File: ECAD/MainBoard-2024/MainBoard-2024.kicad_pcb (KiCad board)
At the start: 2 copper layers, 60 x 150 mm, 82 parts, among them J1 XT60, J10 Conn_01x14, J11 Conn_01x03, J12 Conn_01x04, J13 Conn_01x03, J14 Conn_01x03, J16 XT30, J17 XT30, J2 Conn_01x04, J20 BAU, J21 BAU, J22 Conn_01x04, J23 Conn_01x02, J26 BAU, J27 BAU, J28 Conn_01x02, J29 Conn_01x02, J3 ConStep1, J30 Conn_01x03, J5 ConStep1, J6 ConStep1, J7 XT30, J8 Conn_01x02, J9 XT60, K1 CB1-P-24V, U1 Teensy3.5_All_Pins, U2 R-78B3.3-2.0, U3 PCA9685PW, U4 R-78B5.0-2.0

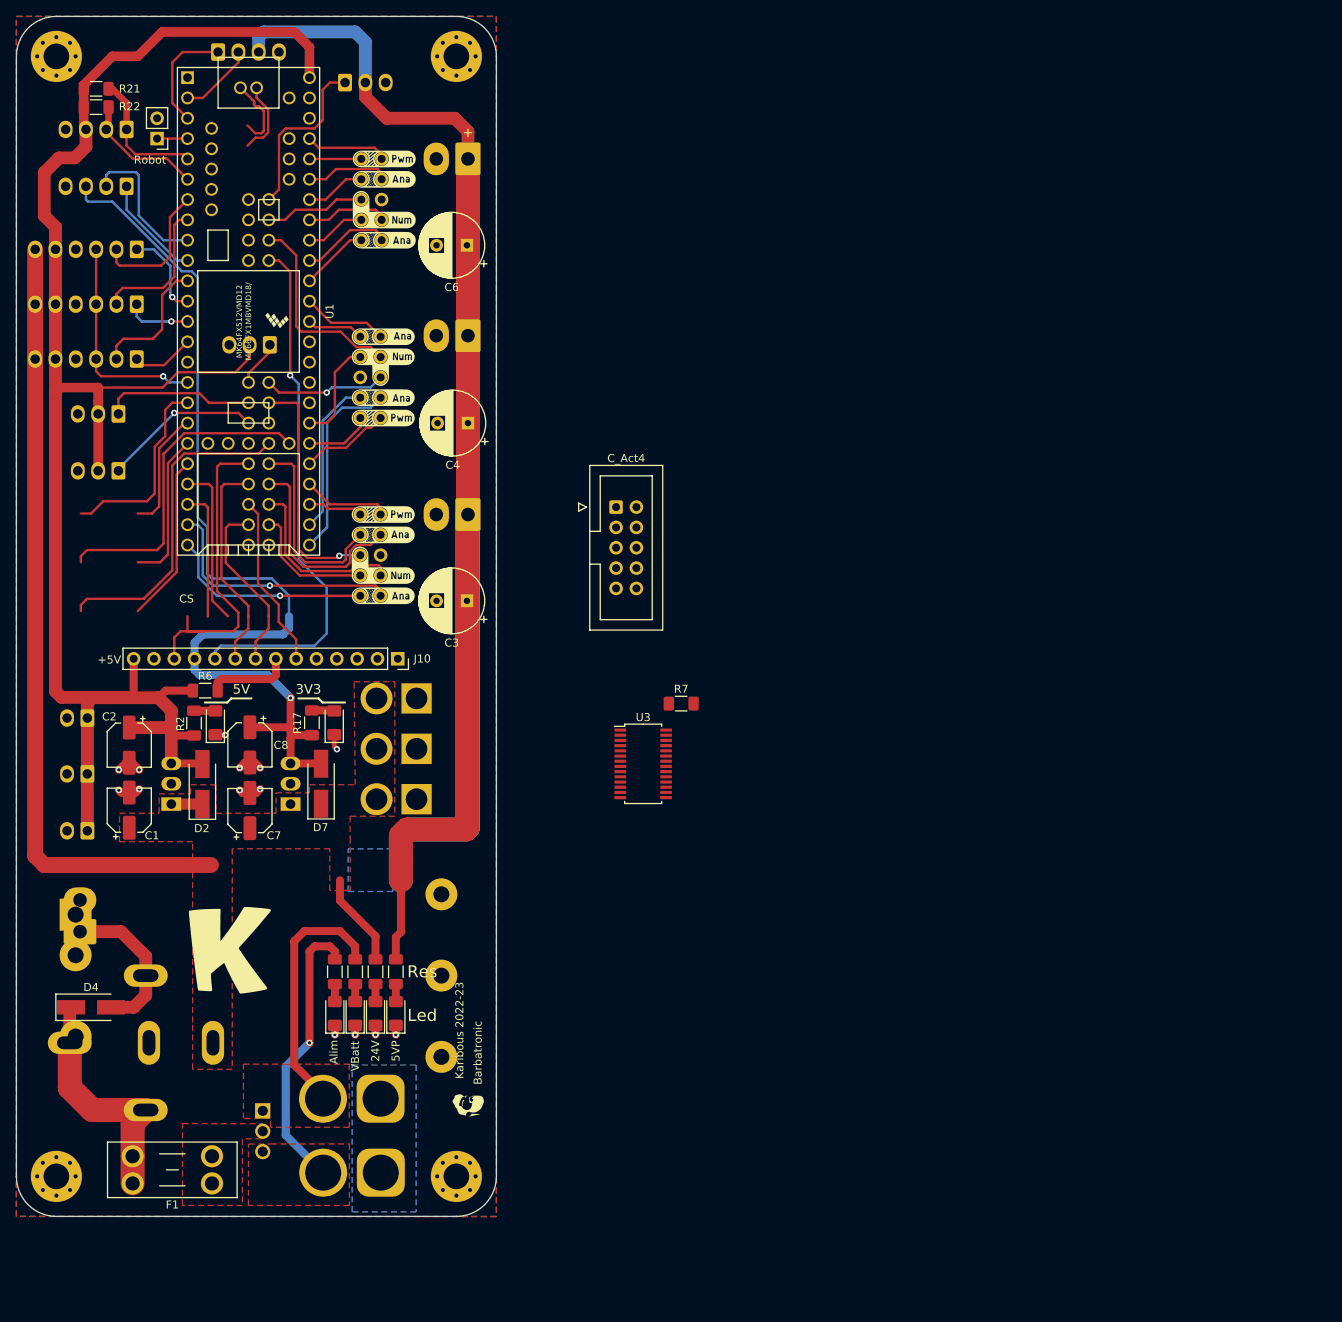
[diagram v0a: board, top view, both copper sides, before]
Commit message: update component and edge cut
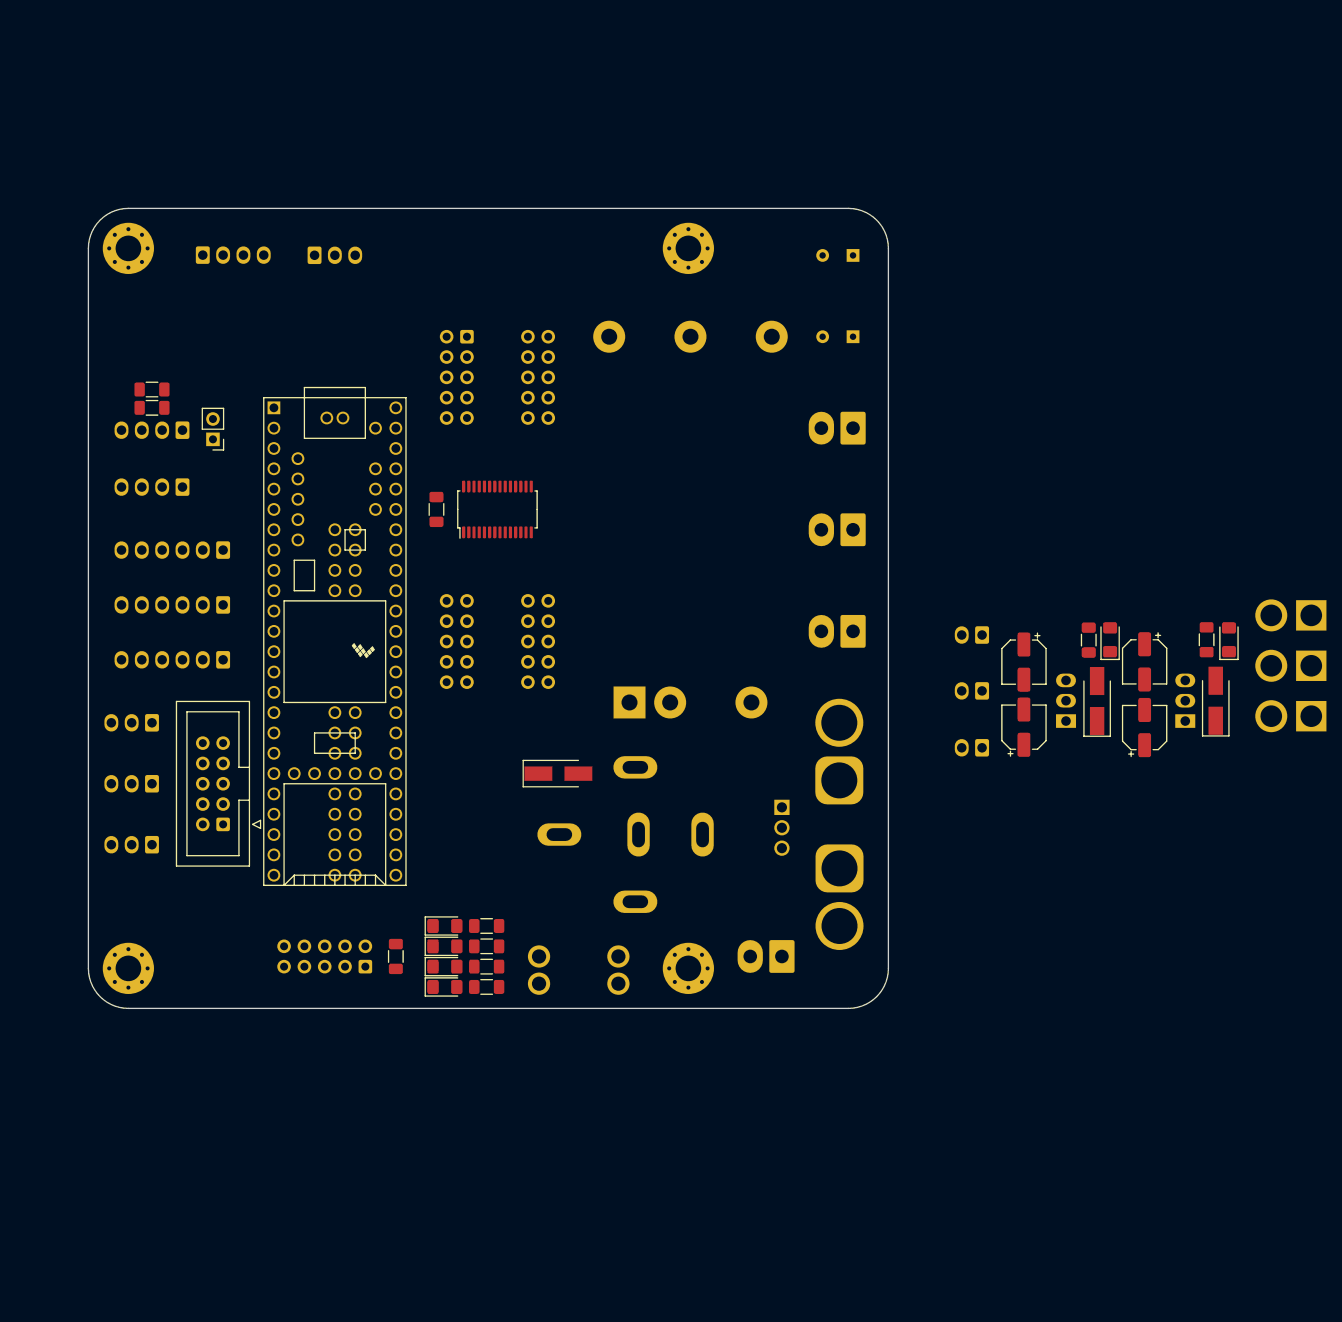
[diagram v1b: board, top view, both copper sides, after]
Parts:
- removed C3: 220uF, Capacitor_THT:CP_Radial_D8.0mm_P3.80mm
- removed G*** (x13): LOGO, LOGO
- removed J10: Conn_01x14, Connector_PinSocket_2.54mm:PinSocket_1x14_P2.54mm_Vertical
- removed kibuzzard-62E65D6B: G***, kibuzzard-62E65D6B
- removed kibuzzard-62E65D77: G***, kibuzzard-62E65D77
- removed kibuzzard-62E65D7D: G***, kibuzzard-62E65D7D
- added Con-TFT1: Conn_02x05_Odd_Even, Connector_IDC:IDC-Header_2x05_P2.54mm_Vertical, B.Cu at (134.6, 144.8)
- added IHM-IO1: Conn_02x05_Odd_Even, Connector_IDC:IDC-Header_2x05_P2.54mm_Vertical, F.Cu at (116.8, 127.0)
- C4, C6, C_Act4, F1: moved to B.Cu
- moved D2 112.3 mm to (226.1, 111.6)
- moved D3 112.3 mm to (227.7, 103.9)
- moved D7 112.3 mm to (240.9, 111.5)
- moved R17 112.3 mm to (239.8, 103.9)
- moved R2 112.3 mm to (225.0, 104.0)
- moved U2 112.3 mm to (237.1, 114.1)
- moved U4 112.3 mm to (222.2, 114.1)
- moved C1 112.3 mm to (216.9, 114.8)
- moved C2 112.3 mm to (216.9, 106.7)
- moved C7 112.3 mm to (232.0, 114.9)
- moved C8 112.3 mm to (232.0, 106.7)
- moved J23 112.3 mm to (211.7, 110.3)
- moved J28 112.3 mm to (211.7, 117.4)
- moved J29 112.3 mm to (211.7, 103.3)
- moved D8 112.3 mm to (242.6, 103.9)
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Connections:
- C_Act1 pad 1: C_Act1-1 -> Act1_01
- C_Act1 pad 10: C_Act1-8 -> Servo03
- C_Act1 pad 2: C_Act1-2 -> Servo00
- C_Act1 pad 3: C_Act1-3 -> Act1_02
- C_Act1 pad 4: C_Act1-4 -> Servo01
- C_Act1 pad 5: C_Act1-9 -> Act1_03
- C_Act1 pad 7: C_Act1-5 -> Act1_04
- C_Act1 pad 8: C_Act1-6 -> Servo02
- C_Act1 pad 9: C_Act1-7 -> Act1_05
- C_Act2 pad 1: C_Act2-8 -> Act2_01
- C_Act2 pad 10: C_Act2-1 -> Servo07
- C_Act2 pad 2: C_Act2-7 -> Servo04
- C_Act2 pad 3: C_Act2-6 -> Act2_02
- C_Act2 pad 4: C_Act2-5 -> Servo05
- C_Act2 pad 5: C_Act2-9 -> Act2_03
- C_Act2 pad 7: C_Act2-4 -> Act2_04
- C_Act2 pad 8: C_Act2-3 -> Servo06
- C_Act2 pad 9: C_Act2-2 -> Act2_05
- C_Act3 pad 1: C_Act3-1 -> Act3_01
- C_Act3 pad 10: C_Act3-8 -> Servo11
- C_Act3 pad 2: C_Act3-2 -> Servo08
- C_Act3 pad 3: C_Act3-3 -> Act3_02
- C_Act3 pad 4: C_Act3-4 -> Servo09
- C_Act3 pad 5: C_Act3-9 -> Act3_03
- C_Act3 pad 7: C_Act3-5 -> Act3_04
- C_Act3 pad 8: C_Act3-6 -> Servo10
- C_Act3 pad 9: C_Act3-7 -> Act3_05
- C_Act4 pad 1: Reset -> Act4_01
- C_Act4 pad 10: unconnected-(C_Act4-Pin_10-Pad10) -> Servo15
- C_Act4 pad 2: Init -> Servo12
- C_Act4 pad 3: Program -> Act4_02
- C_Act4 pad 4: unconnected-(C_Act4-Pin_4-Pad4) -> Servo13
- C_Act4 pad 5: Detection -> Act4_03
- C_Act4 pad 7: Couleur -> Act4_04
- C_Act4 pad 8: unconnected-(C_Act4-Pin_8-Pad8) -> Servo14
- C_Act4 pad 9: Tirette -> Act4_05
- U1 pad 23: C_Act3-2 -> unconnected-(U1-31_A12_RX4_CS1-Pad23)
- U1 pad 24: C_Act3-1 -> unconnected-(U1-32_A13_TX4_SCK1-Pad24)
- U1 pad 28: Program -> unconnected-(U1-Program-Pad28)
- U1 pad 29: Reset -> unconnected-(U1-Reset-Pad29)
- U1 pad 30: C_Act2-4 -> unconnected-(U1-33_A14_TX5_CAN1TX_SCL0-Pad30)
- U1 pad 31: C_Act2-3 -> unconnected-(U1-34_A15_RX5_CAN1RX_SDA0-Pad31)
- U1 pad 32: C_Act3-7 -> unconnected-(U1-35_A16_PWM-Pad32)
- U1 pad 33: C_Act3-8 -> unconnected-(U1-36_A17_PWM-Pad33)
- U1 pad 34: C_Act2-2 -> unconnected-(U1-37_A18_PWM_SCL1-Pad34)
- U1 pad 35: C_Act2-1 -> unconnected-(U1-38_A19_PWM_SDA1-Pad35)
- U1 pad 36: C_Act2-5 -> unconnected-(U1-39_A20-Pad36)
- U1 pad 41: C_Act2-7 -> unconnected-(U1-14_A0_PWM_SCK0-Pad41)
- U1 pad 42: C_Act2-8 -> unconnected-(U1-15_A1_CS0_Touch-Pad42)
- U1 pad 43: C_Act1-1 -> unconnected-(U1-16_A2_SCL0_Touch-Pad43)
- U1 pad 44: C_Act1-2 -> unconnected-(U1-17_A3_SDA0_Touch-Pad44)
- U1 pad 45: C_Act1-3 -> unconnected-(U1-18_A4_SDA0_Touch-Pad45)
- U1 pad 46: C_Act1-4 -> unconnected-(U1-19_A5_SCL0_Touch-Pad46)
- U1 pad 47: C_Act1-5 -> unconnected-(U1-20_A6_PWM_CS0_SCK1-Pad47)
- U1 pad 48: C_Act1-6 -> unconnected-(U1-21_A7_PWM_CS0_MOSI1-Pad48)
- U1 pad 49: C_Act1-7 -> unconnected-(U1-22_A8_PWM_Touch-Pad49)
- U1 pad 50: C_Act1-8 -> unconnected-(U1-23_A9_PWM_Touch-Pad50)
- U1 pad 76: C_Act3-3 -> unconnected-(U1-47_RX6_SCL0-Pad76)
- U1 pad 77: C_Act3-4 -> unconnected-(U1-48_TX6_SDA0-Pad77)
- U1 pad 78: C_Act3-6 -> unconnected-(U1-49_A23-Pad78)
- U1 pad 79: C_Act3-5 -> unconnected-(U1-50_A24-Pad79)
- U1 pad 81: C_Act3-9 -> unconnected-(U1-52_MOSI2-Pad81)
- U1 pad 82: C_Act2-9 -> unconnected-(U1-53_SCK2-Pad82)
- U1 pad 84: C_Act2-6 -> unconnected-(U1-55-Pad84)
- U1 pad 85: C_Act1-9 -> unconnected-(U1-56-Pad85)
- U3 pad 10: unconnected-(U3-SERVO4-Pad10) -> Servo04
- U3 pad 11: unconnected-(U3-SERVO5-Pad11) -> Servo05
- U3 pad 12: unconnected-(U3-SERVO6-Pad12) -> Servo06
- U3 pad 13: unconnected-(U3-SERVO7-Pad13) -> Servo07
- U3 pad 15: unconnected-(U3-SERVO8-Pad15) -> Servo08
- U3 pad 16: unconnected-(U3-SERVO9-Pad16) -> Servo09
- U3 pad 17: unconnected-(U3-SERVO10-Pad17) -> Servo10
- U3 pad 18: unconnected-(U3-SERVO11-Pad18) -> Servo11
- U3 pad 19: unconnected-(U3-SERVO12-Pad19) -> Servo12
- U3 pad 20: unconnected-(U3-SERVO13-Pad20) -> Servo13
- U3 pad 21: unconnected-(U3-SERVO14-Pad21) -> Servo14
- U3 pad 22: unconnected-(U3-SERVO15-Pad22) -> Servo15
- U3 pad 6: unconnected-(U3-SERVO0-Pad6) -> Servo00
- U3 pad 7: unconnected-(U3-SERVO1-Pad7) -> Servo01
- U3 pad 8: unconnected-(U3-SERVO2-Pad8) -> Servo02
- U3 pad 9: unconnected-(U3-SERVO3-Pad9) -> Servo03
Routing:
- net +5VP: track 246.9 -> 0.00 mm
- net +5V: track 220.2 -> 0.00 mm
- net +3V3: track 122.1 -> 0.00 mm, vias 1 -> 0
- net +24V: track 113.9 -> 0.00 mm
- net TFT_DC: track 66.2 -> 0.00 mm, vias 1 -> 0
- net TFT_CS: track 40.3 -> 0.00 mm
- net Program: track 40.3 -> 0.00 mm
- net Reset: track 40.3 -> 0.00 mm
- net ALIM: track 35.5 -> 0.00 mm, vias 1 -> 0
- net C_Act3-2: track 31.5 -> 0.00 mm, vias 1 -> 0
- net +BATT: track 31.1 -> 0.00 mm
- net Net-(D4-K): track 30.6 -> 0.00 mm
- net C_Act3-9: track 30.2 -> 0.00 mm, vias 1 -> 0
- net EN: track 27.2 -> 0.00 mm, vias 1 -> 0
- net TFT_MOSI: track 27.1 -> 0.00 mm
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- removed copper zone on F.Cu, net +24V
- removed copper zone on F.Cu, net +BATT
- removed copper zone on F.Cu, net /24VD
- removed copper zone on F.Cu, net ALIM
- removed copper zone on B.Cu, net GND
- removed copper zone on F.Cu, net GND
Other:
- board size 60 x 150 mm -> 100 x 100 mm
- board text removed: "+"
- board text removed: "+5V"
- board text removed: "-"
- board text removed: "24V"
- board text removed: "3V3"
- board text removed: "3V3 Reg."
- board text removed: "5V"
- board text removed: "5V Reg."
- board text removed: "5VP"
- board text removed: "Alim"
- board text removed: "Alim ext."
- board text removed: "Arrêt d'urgence"
- board text removed: "Barbatronic"
- board text removed: "Batterie"
- board text removed: "CS"
- board text removed: "Connecteur Actionneurs"
- board text removed: "D+"
- board text removed: "D-"
- board text removed: "DC"
- board text removed: "Detec"
- board text removed: "Dir"
- board text removed: "En"
- board text removed: "I2C"
- board text removed: "Init"
- board text removed: "Karibous 2022-23"
- board text removed: "Led"
- board text removed: "Lidar"
- board text removed: "Miso"
- board text removed: "Mosi"
- board text removed: "NeoPixel"
- board text removed: "Progr"
- board text removed: "Res"
- board text removed: "Reset"
- board text removed: "Robot"
- board text removed: "SCK"
- board text removed: "SCL"
- board text removed: "SDA"
- board text removed: "Sensor 01"
- board text removed: "Sensor 02"
- board text removed: "Sensor 03"
- board text removed: "Sig"
- board text removed: "St"
- board text removed: "Team"
- board text removed: "Tirette"
- board text removed: "USB"
- board text removed: "VBatt"
- board text removed: "Xbee"

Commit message: Simplify + add 12V regul
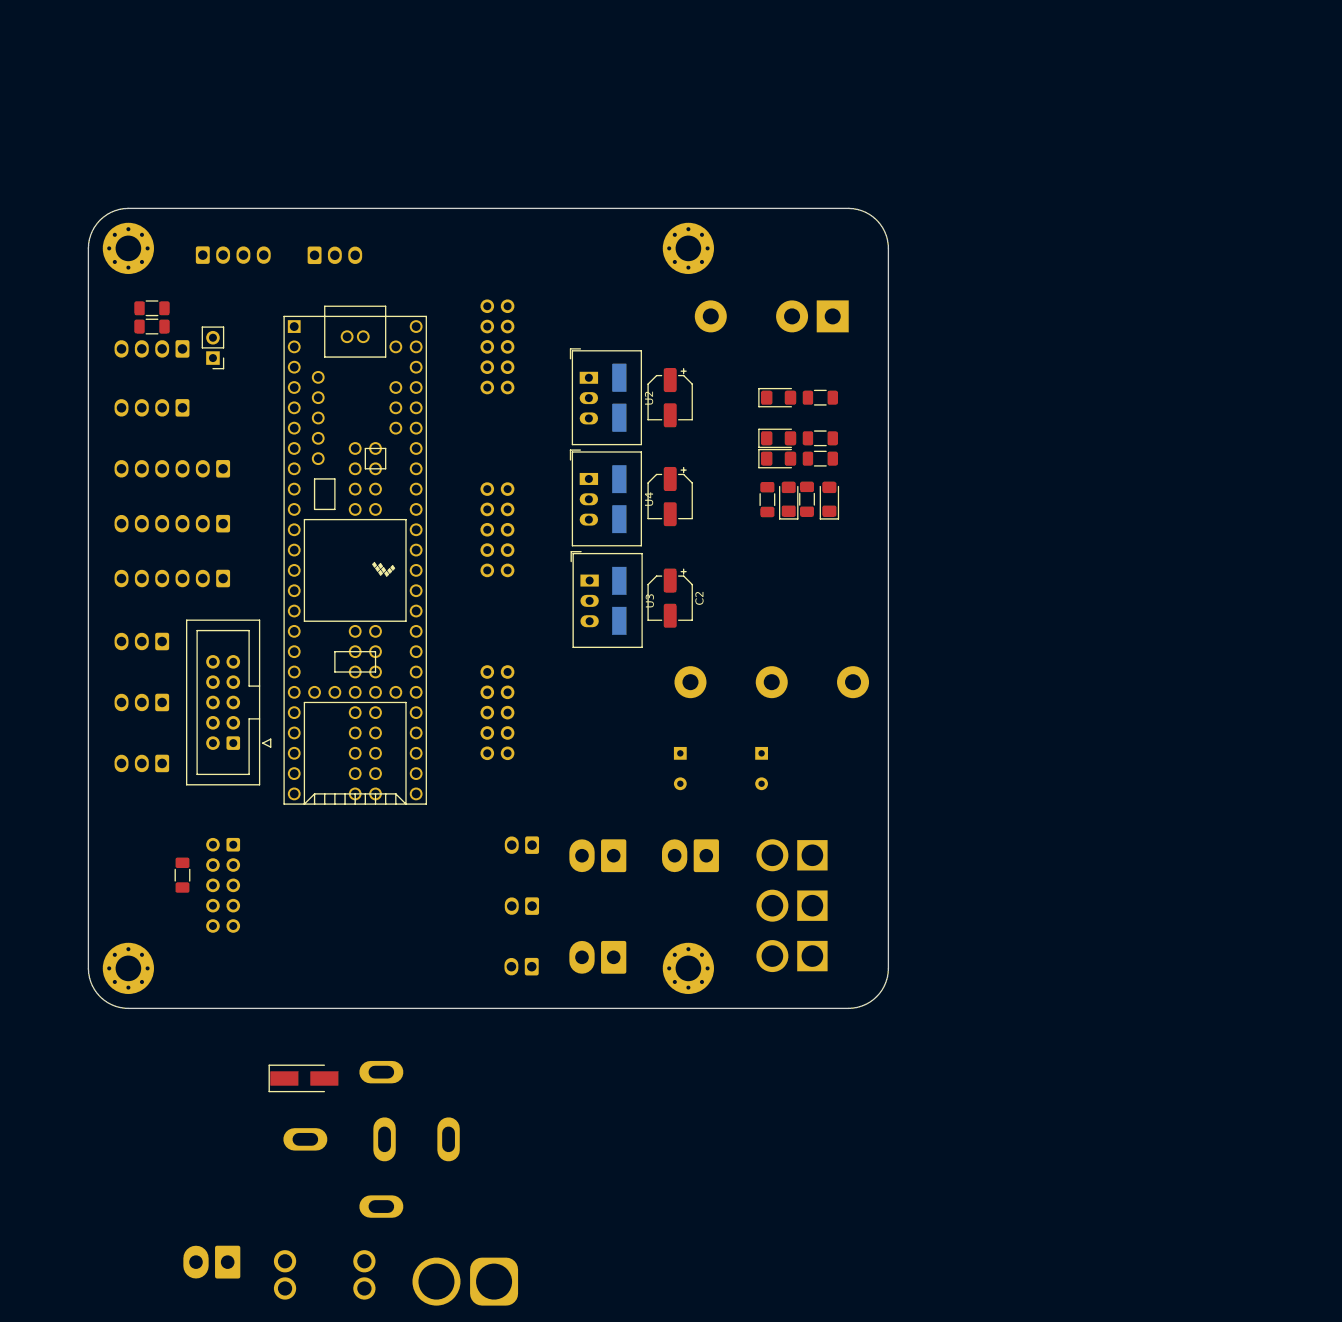
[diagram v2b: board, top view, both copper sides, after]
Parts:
- removed C8: CP_Small, Capacitor_SMD:CP_Elec_5x5.4
- removed C_Act4: Conn_02x05_Odd_Even, Connector_IDC:IDC-Header_2x05_P2.54mm_Vertical
- removed D10: D_Dual_CommonCathode_AKA_Parallel, byv34-400:BYV34-400
- removed J9: XT60, Connector_AMASS:AMASS_XT60-M_1x02_P7.20mm_Vertical
- removed R5: R_Small, Resistor_SMD:R_1206_3216Metric_Pad1.30x1.75mm_HandSolder
- removed R7: 10K, Resistor_SMD:R_1206_3216Metric_Pad1.30x1.75mm_HandSolder
- C1, C2, C7: value CP_Small -> 22uF
- D2, D7: moved to B.Cu
- D9: value LED_Small -> D_Small; footprint LED_SMD:LED_1206_3216Metric_Pad1.42x1.75mm_HandSolder -> Diode_SMD:D_SMA_Handsoldering; moved to B.Cu
- U2, U4: footprint Converter_DCDC:Converter_DCDC_RECOM_R-78B-2.0_THT -> Converter_DCDC:Converter_DCDC_RECOM_R-78E-0.5_THT; moved to F.Cu
- U3: value PCA9685PW -> R-78B12-2.0; footprint Package_SO:TSSOP-28_4.4x9.7mm_P0.65mm -> Converter_DCDC:Converter_DCDC_RECOM_R-78E-0.5_THT
- moved U2 86.0 mm to (162.6, 71.2), turned to -90 degrees
- moved D7 83.6 mm to (166.4, 73.7), turned to -90 degrees
- moved J21 79.1 mm to (117.4, 181.7)
- moved D5 78.1 mm to (186.3, 78.7)
- moved R3 78.1 mm to (191.5, 78.7)
- moved D1 78.1 mm to (186.3, 81.3)
- moved D6 78.1 mm to (186.3, 73.7)
- moved R1 78.1 mm to (191.5, 81.3)
- moved R4 78.1 mm to (191.5, 73.7)
- moved J1 76.1 mm to (150.7, 184.2), turned to 180 degrees
- moved C7 72.2 mm to (172.7, 73.7), turned to -90 degrees
- moved J16 69.2 mm to (190.5, 130.9)
- moved J17 69.2 mm to (190.5, 137.2)
- moved J7 69.2 mm to (190.5, 143.5)
- moved U4 66.9 mm to (162.6, 83.8), turned to -90 degrees
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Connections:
- C2 pad 1: +5V -> +24V
- C_Act1 pad 1: Act1_01 -> C_Act1-1
- C_Act1 pad 10: Servo03 -> C_Act1-8
- C_Act1 pad 2: Servo00 -> C_Act1-2
- C_Act1 pad 3: Act1_02 -> C_Act1-3
- C_Act1 pad 4: Servo01 -> C_Act1-4
- C_Act1 pad 5: Act1_03 -> C_Act1-9
- C_Act1 pad 7: Act1_04 -> C_Act1-5
- C_Act1 pad 8: Servo02 -> C_Act1-6
- C_Act1 pad 9: Act1_05 -> C_Act1-7
- C_Act2 pad 1: Act2_01 -> C_Act2-8
- C_Act2 pad 10: Servo07 -> C_Act2-1
- C_Act2 pad 2: Servo04 -> C_Act2-7
- C_Act2 pad 3: Act2_02 -> C_Act2-6
- C_Act2 pad 4: Servo05 -> C_Act2-5
- C_Act2 pad 5: Act2_03 -> C_Act2-9
- C_Act2 pad 7: Act2_04 -> C_Act2-4
- C_Act2 pad 8: Servo06 -> C_Act2-3
- C_Act2 pad 9: Act2_05 -> C_Act2-2
- C_Act3 pad 1: Act3_01 -> C_Act3-1
- C_Act3 pad 10: Servo11 -> C_Act3-8
- C_Act3 pad 2: Servo08 -> C_Act3-2
- C_Act3 pad 3: Act3_02 -> C_Act3-3
- C_Act3 pad 4: Servo09 -> C_Act3-4
- C_Act3 pad 5: Act3_03 -> C_Act3-9
- C_Act3 pad 7: Act3_04 -> C_Act3-5
- C_Act3 pad 8: Servo10 -> C_Act3-6
- C_Act3 pad 9: Act3_05 -> C_Act3-7
- D9 pad 1: GND -> +24V
- D9 pad 2: Net-(D9-A) -> +12V
- F1 pad 1: /24VD -> +BATT
- PS1 pad 2: unconnected-(PS1--VIN(GND)-Pad2) -> GND
- U1 pad 23: unconnected-(U1-31_A12_RX4_CS1-Pad23) -> C_Act3-2
- U1 pad 24: unconnected-(U1-32_A13_TX4_SCK1-Pad24) -> C_Act3-1
- U1 pad 30: unconnected-(U1-33_A14_TX5_CAN1TX_SCL0-Pad30) -> C_Act2-4
- U1 pad 31: unconnected-(U1-34_A15_RX5_CAN1RX_SDA0-Pad31) -> C_Act2-3
- U1 pad 32: unconnected-(U1-35_A16_PWM-Pad32) -> C_Act3-7
- U1 pad 33: unconnected-(U1-36_A17_PWM-Pad33) -> C_Act3-8
- U1 pad 34: unconnected-(U1-37_A18_PWM_SCL1-Pad34) -> C_Act2-2
- U1 pad 35: unconnected-(U1-38_A19_PWM_SDA1-Pad35) -> C_Act2-1
- U1 pad 36: unconnected-(U1-39_A20-Pad36) -> C_Act2-5
- U1 pad 41: unconnected-(U1-14_A0_PWM_SCK0-Pad41) -> C_Act2-7
- U1 pad 42: unconnected-(U1-15_A1_CS0_Touch-Pad42) -> C_Act2-8
- U1 pad 43: unconnected-(U1-16_A2_SCL0_Touch-Pad43) -> C_Act1-1
- U1 pad 44: unconnected-(U1-17_A3_SDA0_Touch-Pad44) -> C_Act1-2
- U1 pad 45: unconnected-(U1-18_A4_SDA0_Touch-Pad45) -> C_Act1-3
- U1 pad 46: unconnected-(U1-19_A5_SCL0_Touch-Pad46) -> C_Act1-4
- U1 pad 47: unconnected-(U1-20_A6_PWM_CS0_SCK1-Pad47) -> C_Act1-5
- U1 pad 48: unconnected-(U1-21_A7_PWM_CS0_MOSI1-Pad48) -> C_Act1-6
- U1 pad 49: unconnected-(U1-22_A8_PWM_Touch-Pad49) -> C_Act1-7
- U1 pad 50: unconnected-(U1-23_A9_PWM_Touch-Pad50) -> C_Act1-8
- U1 pad 76: unconnected-(U1-47_RX6_SCL0-Pad76) -> C_Act3-3
- U1 pad 77: unconnected-(U1-48_TX6_SDA0-Pad77) -> C_Act3-4
- U1 pad 78: unconnected-(U1-49_A23-Pad78) -> C_Act3-6
- U1 pad 79: unconnected-(U1-50_A24-Pad79) -> C_Act3-5
- U1 pad 81: unconnected-(U1-52_MOSI2-Pad81) -> C_Act3-9
- U1 pad 82: unconnected-(U1-53_SCK2-Pad82) -> C_Act2-9
- U1 pad 84: unconnected-(U1-55-Pad84) -> C_Act2-6
- U1 pad 85: unconnected-(U1-56-Pad85) -> C_Act1-9
- U3 pad 1: GND -> +24V
- U3 pad 3: GND -> +12V

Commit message: change relay
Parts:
- removed K1: CB1-P-24V, CB1-P-24V:Panasonic_Electric_Works-CB1-P-24V-MFG
- added K2: FINDER-36.11, Relay_THT:Relay_SPDT_Finder_36.11, B.Cu at (178.2, 131.7)
- F1: moved to F.Cu
- IHM-IO1: moved to B.Cu
- moved J21 87.8 mm to (177.9, 118.1)
- moved J1 59.4 mm to (194.1, 143.5)
- moved D4 51.9 mm to (171.4, 132.0), turned to -90 degrees
- moved F1 43.7 mm to (155.1, 143.1), turned to 0 degrees
- moved J20 22.0 mm to (143.7, 130.8)
- moved J23 22.0 mm to (133.5, 137.1)
- moved J26 22.0 mm to (155.2, 130.8)
- moved J27 22.0 mm to (143.7, 143.5)
- moved J28 22.0 mm to (133.4, 144.7)
- moved J29 22.0 mm to (133.5, 129.5)
- moved C6 20.1 mm to (166.4, 108.7)
- moved C4 12.8 mm to (161.3, 116.8)
- moved IHM-IO1 10.2 mm to (118.1, 106.7)
- moved J16 9.64 mm to (194.2, 122.0)
- moved J7 9.64 mm to (194.2, 134.6)
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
